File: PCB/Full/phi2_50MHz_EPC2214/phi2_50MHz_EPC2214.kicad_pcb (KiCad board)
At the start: 2 copper layers, 54 parts, among them J1 RF_IN, J2 RF_OUT, J5 Conn_01x01_Pin, J6 Conn_01x01_Pin, Q1 EPC2214, U1 TPS563203, U2 NC7WZ04, U3 NC7WZ04, U4 TLV3501, U5 NC7WZ04, U6 NC7WZ04, U7 NC7WZ04

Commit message: rough draft of phi 2 board
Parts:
- removed C16: C_Small, Capacitor_SMD:C_1206_3216Metric
- removed C30: C, Capacitor_SMD:C_0402_1005Metric
- removed U2: NC7WZ04, pcbparts:nc7wz04_sc-88_SOIC-6
- added D1: SMS3922, Diode_SMD:D_SOD-523, F.Cu at (134.7, 90.7)
- added D2: RB886GT2R, Diode_SMD:D_SOD-523, F.Cu at (134.7, 92.1)
- added D3: RB886GT2R, Diode_SMD:D_SOD-523, F.Cu at (134.7, 93.5)
- added D4: RB886GT2R, Diode_SMD:D_SOD-523, F.Cu at (134.7, 94.9)
- added D5: RB886GT2R, Diode_SMD:D_SOD-523, F.Cu at (137.3, 90.7)
- added D6: RB886GT2R, Diode_SMD:D_SOD-523, F.Cu at (137.3, 92.1)
- added D7: RB886GT2R, Diode_SMD:D_SOD-523, F.Cu at (137.3, 93.5)
- added D8: RB886GT2R, Diode_SMD:D_SOD-523, F.Cu at (137.3, 94.9)
- added REF**: MountingHole_4.3mm_M4_DIN965, MountingHole:MountingHole_4.3mm_M4_DIN965, F.Cu at (164.7, 61.8)
- added REF**: MountingHole_4.3mm_M4_DIN965, MountingHole:MountingHole_4.3mm_M4_DIN965, F.Cu at (106.7, 61.8)
- added REF**: MountingHole_4.3mm_M4_DIN965, MountingHole:MountingHole_4.3mm_M4_DIN965, F.Cu at (164.7, 119.8)
- added REF**: MountingHole_4.3mm_M4_DIN965, MountingHole:MountingHole_4.3mm_M4_DIN965, F.Cu at (106.7, 119.8)
- 12 V: renamed from J5
- C10: footprint Capacitor_SMD:C_0603_1608Metric -> Capacitor_SMD:C_0402_1005Metric
- moved RF_IN 86.4 mm to (136.3, 118.6), turned to 90 degrees
- moved GND 84.6 mm to (135.5, 74.3)
- moved C10 78.2 mm to (133.1, 111.8), turned to -90 degrees
- moved U4 75.3 mm to (135.3, 110.9), turned to 90 degrees
- moved R4 73.3 mm to (135.5, 113.7)
- moved C1 73.2 mm to (124.4, 70.9)
- moved R5 72.4 mm to (137.8, 110.9), turned to -90 degrees
- moved U3 70.1 mm to (135.9, 107.0), turned to 0 degrees
- moved R6 68.0 mm to (132.4, 113.7), turned to 180 degrees
- moved U5 63.5 mm to (133.6, 103.5), turned to 0 degrees
- moved U7 63.3 mm to (138.3, 103.5), turned to 0 degrees
- moved U6 63.2 mm to (135.9, 103.5), turned to 0 degrees
- moved C9 60.7 mm to (137.6, 107.5), turned to 90 degrees
- moved C4 60.7 mm to (124.5, 80.7), turned to 0 degrees
- moved C11 59.0 mm to (139.9, 104.1), turned to 90 degrees
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- renumbered J6 to GND, J1 to RF_IN, J2 to RF_OUT
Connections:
- C13 pad 1: Net-(C13-Pad1) -> /D
- C14 pad 1: Net-(C13-Pad1) -> /D
- C15 pad 1: Net-(C13-Pad2) -> /D
- C19 pad 1: Net-(C13-Pad2) -> /D
- C20 pad 1: Net-(C13-Pad2) -> /D
- L1 pad 2: Net-(C13-Pad1) -> /D
- L2 pad 1: Net-(C13-Pad1) -> /D
- Q1 pad 4: Net-(C13-Pad1) -> /D
- Q1 pad 5: Net-(C13-Pad1) -> /D
- Q1 pad 6: Net-(C13-Pad1) -> /D
- Q1 pad 7: Net-(C13-Pad1) -> /D
- U5 pad 4: /G -> /G1
- U5 pad 6: /G -> /G1
- U6 pad 4: /G -> /G1
- U6 pad 6: /G -> /G1
- U7 pad 4: /G -> /G1
- U7 pad 6: /G -> /G1
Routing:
- net +5V: track 0.00 -> 83.7 mm
- net /G1: track 0.00 -> 14.5 mm
- net Net-(U3-Y1): track 0.00 -> 13.0 mm
- net Net-(J2-In): track 0.00 -> 10.6 mm, vias 0 -> 7
- net Net-(U1-SW): track 0.00 -> 10.0 mm, vias 0 -> 2
- net Net-(U4--IN): track 0.00 -> 6.66 mm
- net /RF_IN: track 0.00 -> 6.63 mm
- net Net-(U1-EN): track 0.00 -> 5.70 mm
- net Net-(U1-FB): track 0.00 -> 4.31 mm
- net /D: track 0.00 -> 2.38 mm, vias 0 -> 12
- net GND: track 0.00 -> 1.68 mm, vias 0 -> 213
- net /G: track 0.00 -> 1.53 mm, vias 0 -> 9
- net Net-(U1-BST): track 0.00 -> 1.43 mm
- net Net-(C5-Pad1): vias 0 -> 3
- net Net-(C13-Pad2): vias 0 -> 6
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- added copper zone on F.Cu, net +12V
- added copper zone on F.Cu, net +5V
- added copper zone on B.Cu, net /D
- added copper zone on F.Cu, net /D
- added copper zone on B.Cu, net /G
- added copper zone on F.Cu, net /G
- added copper zone on F.Cu, net /G1
- added copper zone on B.Cu, net GND
- added copper zone on F.Cu, net GND
- added copper zone on B.Cu, net Net-(C12-Pad1)
- added copper zone on F.Cu, net Net-(C12-Pad1)
- added copper zone on B.Cu, net Net-(C13-Pad2)
- added copper zone on F.Cu, net Net-(C13-Pad2)
- added copper zone on B.Cu, net Net-(C5-Pad1)
- added copper zone on F.Cu, net Net-(C5-Pad1)
- added copper zone on B.Cu, net Net-(J2-In)
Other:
- board outline added: 70 x 70 mm
- board text added: "IMSSDC 6 50 MHz GaN PA CALVIN H LIN, ZHECHI YE"

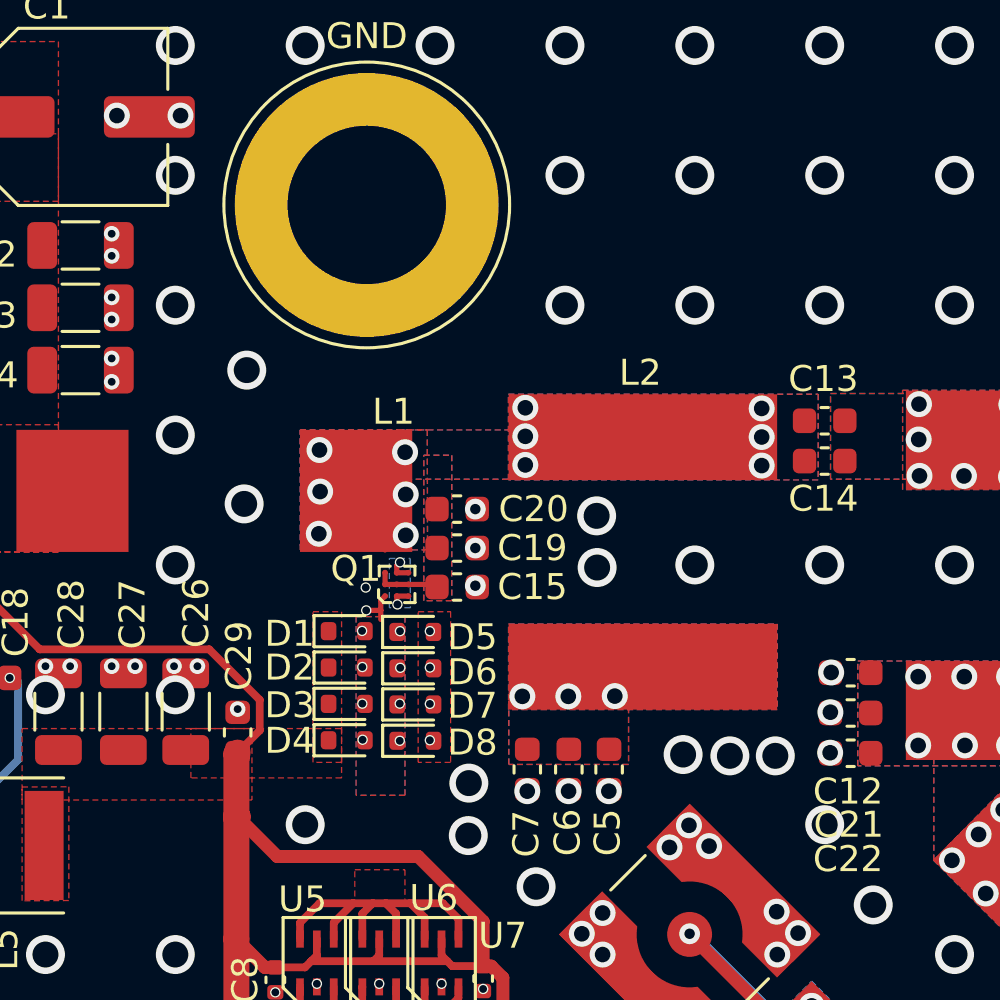
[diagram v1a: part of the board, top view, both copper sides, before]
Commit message: deleted some vias
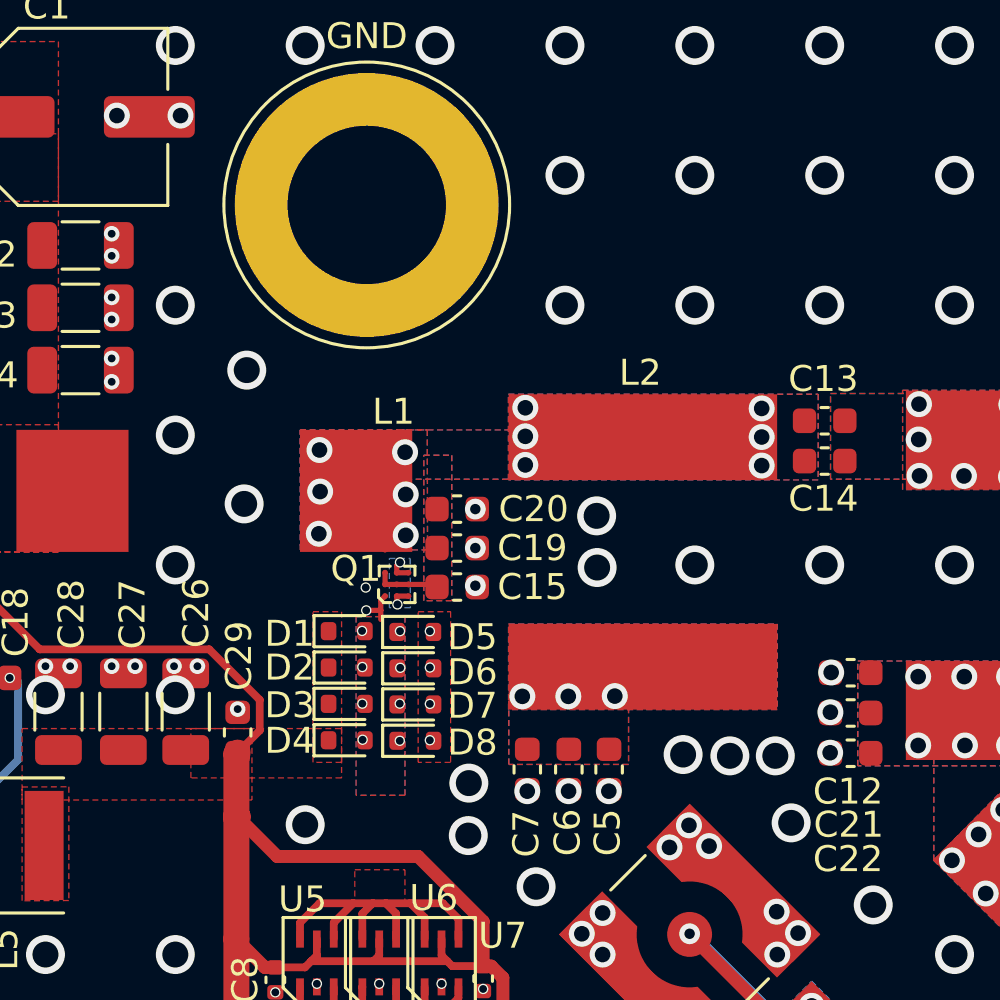
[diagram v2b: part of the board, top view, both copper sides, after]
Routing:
- net GND: vias 213 -> 212
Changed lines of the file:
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@@
 	)
 	(via
-		(at 153.1 98.15)
+		(at 151.81 98.08)
 		(size 1.5)
 		(drill 1)
@@
 		(size 1.5)
 		(drill 1)
-		(layers "F.Cu" "B.Cu")
-		(free yes)
-		(net 1)
-	)
-	(via
-		(at 128.1 73.15)
-		(size 1.5)
-		(drill 1)

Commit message: gerbers and rev1 board sent out
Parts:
- removed the REF** at (164.7, 61.8)
- removed the REF** at (106.7, 61.8)
- removed the REF** at (164.7, 119.8)
- removed the REF** at (106.7, 119.8)
- added G***: LOGO, Logo:superlab_logo, F.Cu at (74.3, 81.8)
- added REF**: MountingHole_3.2mm_M3_DIN965, MountingHole:MountingHole_3.2mm_M3_DIN965, F.Cu at (4.67, 84.8)
- added REF**: MountingHole_3.2mm_M3_DIN965, MountingHole:MountingHole_3.2mm_M3_DIN965, F.Cu at (84.7, 41.7)
- added REF**: MountingHole_3.2mm_M3_DIN965, MountingHole:MountingHole_3.2mm_M3_DIN965, F.Cu at (84.7, 3.80)
- added REF**: MountingHole_3.2mm_M3_DIN965, MountingHole:MountingHole_3.2mm_M3_DIN965, F.Cu at (4.67, 3.80)
- added REF**: MountingHole_3.2mm_M3_DIN965, MountingHole:MountingHole_3.2mm_M3_DIN965, F.Cu at (84.7, 84.8)
- added REF**: MountingHole_3.2mm_M3_DIN965, MountingHole:MountingHole_3.2mm_M3_DIN965, F.Cu at (4.67, 41.7)
- moved C15 108.3 mm to (45.6, 34.0), turned to -90 degrees
- moved C1 107.4 mm to (31.8, 16.6)
- moved C10 107.4 mm to (40.4, 57.5)
- moved C25 107.4 mm to (24.8, 42.5)
- moved C5 107.4 mm to (52.2, 41.7)
- moved R5 107.4 mm to (45.2, 56.6)
- moved RF_IN 107.4 mm to (43.7, 64.3)
- moved U4 107.4 mm to (42.7, 56.6)
- moved U5 107.4 mm to (40.9, 49.2)
- moved 12 V 107.4 mm to (21.2, 15.7)
- moved C11 107.4 mm to (47.3, 49.8)
- moved C12 107.4 mm to (61.5, 38.0)
- moved C13 107.4 mm to (60.5, 28.3)
- moved C14 107.4 mm to (60.5, 29.9)
- moved C17 107.4 mm to (41.5, 53.3)
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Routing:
- net +12V: track 0.19 -> 6.13 mm, vias 0 -> 2
- net Net-(J2-In): track 10.6 -> 5.35 mm, vias 7 -> 0
- net +5V: track 83.7 -> 85.7 mm
- net Net-(U3-A1): track 0.00 -> 1.98 mm
- net GND: track 1.68 -> 1.91 mm, vias 212 -> 210
- net /D: track 2.38 -> 2.61 mm, vias 12 -> 0
- net Net-(C5-Pad1): vias 3 -> 0
- net Net-(C13-Pad2): vias 6 -> 0
- net Net-(C12-Pad1): vias 12 -> 0
- added copper zone on F.Cu, net Net-(J2-In)
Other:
- board size 70 x 70 mm -> 89 x 89 mm
- board text added: "IMSSDC 6 2024 50 MHz GaN PA CALVIN H LIN, ZHECHI YE STANFORD POWER ELECTRONICS"
- board text removed: "IMSSDC 6 50 MHz GaN PA CALVIN H LIN, ZHECHI YE"

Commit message: added width to drain trace, now sent out board
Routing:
- net /D: track 2.61 -> 4.05 mm
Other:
- board text added: "IMS SDC6 2024 50 MHz GaN PA CALVIN H LIN, ZHECHI YE STANFORD POWER ELECTRONICS"
- board text removed: "IMSSDC 6 2024 50 MHz GaN PA CALVIN H LIN, ZHECHI YE STANFORD POWER ELECTRONICS"
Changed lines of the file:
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@@
 			(fill solid)
 			(layer "F.SilkS")
-			(net 45360009)
 		)
 		(fp_poly
@@
 		(layer "Edge.Cuts")
 	)
-	(gr_text "IMSSDC 6 2024\n50 MHz GaN PA\nCALVIN H LIN, ZHECHI YE\nSTANFORD POWER ELECTRONICS"
+	(gr_text "IMS SDC6 2024\n50 MHz GaN PA\nCALVIN H LIN, ZHECHI YE\nSTANFORD POWER ELECTRONICS"
 		(at 45.855 85.35 0)
 		(layer "F.SilkS")
@@
 	)
 	(via
-		(at 42.78 34.23)
+		(at 42.48 34.36)
 		(size 0.4)
 		(drill 0.3)
@@
 	)
 	(segment
+		(start 42.41 31.11)
+		(end 43.43 32.13)
+		(width 0.5)
+		(layer "F.Cu")
+		(net 6)
+	)
+	(segment
 		(start 45.74 33.17)
 		(end 45.71 33.2)
@@
 	)
 	(zone
+		(net 9)
+		(net_name "Net-(U1-SW)")
+		(layer "F.Cu")
+		(name "$teardrop_padvia$")
+		(hatch full 0.1)
+		(priority 30000)
+		(attr
+			(teardrop
+				(type padvia)
+			)
+		)
+		(connect_pads yes
+			(clearance 0)
+		)
+		(min_thickness 0.0254)
+		(filled_areas_thickness no)
+		(fill yes
+			(thermal_gap 0.5)
+			(thermal_bridge_width 0.5)
+			(island_removal_mode 1)
+			(island_area_min 10)
+		)
+		(polygon
+			(pts
+				(xy 26.57 41.69) (xy 26.87 41.69) (xy 26.89 41.435) (xy 26.72 41.169) (xy 26.55 41.435)
+			)
+		)
+	)
+	(zone
 		(net 1)
 		(net_name "GND")
@@
 	)
 	(zone
-		(net 9)
-		(net_name "Net-(U1-SW)")
+		(net 2)
+		(net_name "+12V")
 		(layer "F.Cu")
-		(name "$teardrop_padvia$")
-		(hatch full 0.1)
-		(priority 30000)
-		(attr
-			(teardrop
-				(type padvia)
-			)
-		)
+		(hatch edge 0.5)
+		(priority 1)
 		(connect_pads yes
-			(clearance 0)
+			(clearance 0.1)
 		)
-		(min_thickness 0.0254)
+		(min_thickness 0.25)
 		(filled_areas_thickness no)
 		(fill yes
 			(thermal_gap 0.5)
 			(thermal_bridge_width 0.5)
-			(island_removal_mode 1)
-			(island_area_min 10)
 		)
 		(polygon
 			(pts
-				(xy 26.57 41.69) (xy 26.87 41.69) (xy 26.89 41.435) (xy 26.72 41.169) (xy 26.55 41.435)
+				(xy 30.97 33.37) (xy 18.97 33.37) (xy 18.97 28.47) (xy 30.97 28.47)
 			)
 		)
 	)
 	(zone
-		(net 2)
-		(net_name "+12V")
+		(net 4)
+		(net_name "+5V")
 		(layer "F.Cu")
 		(hatch edge 0.5)
-		(priority 1)
 		(connect_pads yes
 			(clearance 0.1)
@@
 		(polygon
 			(pts
-				(xy 30.97 33.37) (xy 18.97 33.37) (xy 18.97 28.47) (xy 30.97 28.47)
+				(xy 41.87 42.07) (xy 36.07 42.07) (xy 36.07 40.17) (xy 41.87 40.17)
 			)
 		)
 	)
 	(zone
-		(net 4)
-		(net_name "+5V")
+		(net 6)
+		(net_name "/D")
 		(layer "F.Cu")
 		(hatch edge 0.5)
+		(priority 7)
 		(connect_pads yes
-			(clearance 0.1)
+			(clearance 0)
 		)
 		(min_thickness 0.25)
@@
 		(polygon
 			(pts
-				(xy 41.87 42.07) (xy 36.07 42.07) (xy 36.07 40.17) (xy 41.87 40.17)
+				(xy 43.09 33.39) (xy 43.65 33.39) (xy 43.65 34.71) (xy 43.09 34.71)
 			)
 		)
@@
 		(polygon
 			(pts
-				(xy 43.42 33.76) (xy 43.66 33.76) (xy 43.66 34.73) (xy 43.42 34.73)
+				(xy 43.09 33.42) (xy 43.68 33.42) (xy 43.68 34.73) (xy 43.09 34.73)
 			)
 		)

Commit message: kicad changes if i ever make a new board
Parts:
- moved R3 0.27 mm to (24.3, 35.1)
- moved R7 0.27 mm to (24.3, 38.2)
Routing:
- net (no net): track 0.00 -> 1.34 mm
- net GND: track 1.91 -> 2.83 mm
- net +12V: track 6.13 -> 5.31 mm, vias 2 -> 1
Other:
- board text added: "Check ground pin of IC does ground need to be connected underneath package? should we use a different 0.1 uF capacitor with higher voltage rating? 4.7 uH"
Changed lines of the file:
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@@
 	(footprint "Resistor_SMD:R_0603_1608Metric"
 		(layer "F.Cu")
-		(at 24.57 38.32 -90)
+		(at 24.32 38.22 -90)
 		(descr "Resistor SMD 0603 (1608 Metric), square (rectangular) end terminal, IPC_7351 nominal, (Body size source: IPC-SM-782 page 72, https://www.pcb-3d.com/wordpress/wp-content/uploads/ipc-sm-782a_amendment_1_and_2.pdf), generated with kicad-footprint-generator")
 		(tags "resistor")
@@
 	(footprint "Resistor_SMD:R_0603_1608Metric"
 		(layer "F.Cu")
-		(at 24.57 35.22 -90)
+		(at 24.32 35.12 -90)
 		(descr "Resistor SMD 0603 (1608 Metric), square (rectangular) end terminal, IPC_7351 nominal, (Body size source: IPC-SM-782 page 72, https://www.pcb-3d.com/wordpress/wp-content/uploads/ipc-sm-782a_amendment_1_and_2.pdf), generated with kicad-footprint-generator")
 		(tags "resistor")
@@
 		)
 	)
+	(gr_text "Check ground pin of IC\ndoes ground need to be connected underneath package?\nshould we use a different 0.1 uF capacitor with higher voltage rating?\n4.7 uH"
+		(at 10.94 101.94 0)
+		(layer "Cmts.User")
+		(effects
+			(font
+				(size 1.5 1.5)
+				(thickness 0.3)
+				(bold yes)
+			)
+			(justify left bottom)
+		)
+	)
+	(segment
+		(start 26.95 40.34)
+		(end 27.08 40.47)
+		(width 0.25)
+		(layer "F.Cu")
+		(net 0)
+	)
+	(segment
+		(start 25.79 40.34)
+		(end 26.95 40.34)
+		(width 0.25)
+		(layer "F.Cu")
+		(net 0)
+	)
 	(segment
 		(start 43.995 35.07)
@@
 	)
 	(segment
+		(start 27.92 41.17)
+		(end 28.07 41.32)
+		(width 0.25)
+		(layer "F.Cu")
+		(net 1)
+	)
+	(segment
 		(start 43.976666 35.346266)
 		(end 43.995 35.327932)
@@
 	)
 	(segment
+		(start 27.22 41.17)
+		(end 27.92 41.17)
+		(width 0.25)
+		(layer "F.Cu")
+		(net 1)
+	)
+	(segment
 		(start 43.995 34.17)
 		(end 44.44 34.17)
@@
 	(segment
 		(start 25.97 36.88)
-		(end 25.97 37.89)
-		(width 0.3)
+		(end 25.145 36.055)
+		(width 0.25)
 		(layer "F.Cu")
 		(net 2)
 	)
 	(segment
-		(start 25.97 37.89)
-		(end 26.01 37.93)
-		(width 0.3)
+		(start 31.645 30.885)
+		(end 31.51 31.02)
+		(width 1.5)
 		(layer "F.Cu")
 		(net 2)
 	)
 	(segment
-		(start 31.645 30.885)
-		(end 31.51 31.02)
-		(width 1.5)
+		(start 24.78 35.15)
+		(end 23.45 35.15)
+		(width 0.25)
+		(layer "F.Cu")
+		(net 2)
+	)
+	(segment
+		(start 25.145 36.055)
+		(end 25.145 35.515)
+		(width 0.25)
 		(layer "F.Cu")
 		(net 2)
@@
 		(net 2)
 	)
-	(via
-		(at 26.15 41.18)
-		(size 0.4)
-		(drill 0.3)
-		(layers "F.Cu" "B.Cu")
+	(segment
+		(start 25.145 35.515)
+		(end 24.78 35.15)
+		(width 0.25)
+		(layer "F.Cu")
 		(net 2)
 	)
 	(via
-		(at 26.01 37.93)
-		(size 0.6)
+		(at 26.15 41.18)
+		(size 0.4)
 		(drill 0.3)
 		(layers "F.Cu" "B.Cu")
-		(free yes)
-		(net 2)
-	)
-	(segment
-		(start 26.01 41.04)
-		(end 26.01 37.93)
-		(width 0.3)
-		(layer "B.Cu")
-		(net 2)
-	)
-	(segment
-		(start 26.15 41.18)
-		(end 26.01 41.04)
-		(width 0.3)
-		(layer "B.Cu")
 		(net 2)
 	)
@@
 	)
 	(zone
-		(net 9)
-		(net_name "Net-(U1-SW)")
-		(layer "F.Cu")
-		(name "$teardrop_padvia$")
-		(hatch full 0.1)
-		(priority 30000)
-		(attr
-			(teardrop
-				(type padvia)
-			)
-		)
-		(connect_pads yes
-			(clearance 0)
-		)
-		(min_thickness 0.0254)
-		(filled_areas_thickness no)
-		(fill yes
-			(thermal_gap 0.5)
-			(thermal_bridge_width 0.5)
-			(island_removal_mode 1)
-			(island_area_min 10)
-		)
-		(polygon
-			(pts
-				(xy 26.57 41.69) (xy 26.87 41.69) (xy 26.89 41.435) (xy 26.72 41.169) (xy 26.55 41.435)
-			)
-		)
-	)
-	(zone
 		(net 1)
 		(net_name "GND")
@@
 			)
 		)
+	)
+	(zone
+		(net 9)
+		(net_name "Net-(U1-SW)")
+		(layer "F.Cu")
+		(name "$teardrop_padvia$")
+		(hatch full 0.1)
+		(priority 30000)
+		(attr
+			(teardrop
+				(type padvia)
+			)
+		)
+		(connect_pads yes
+			(clearance 0)
+		)
+		(min_thickness 0.0254)
+		(filled_areas_thickness no)
+		(fill yes
+			(thermal_gap 0.5)
+			(thermal_bridge_width 0.5)
+			(island_removal_mode 1)
+			(island_area_min 10)
+		)
+		(polygon
+			(pts
+				(xy 26.57 41.69) (xy 26.87 41.69) (xy 26.89 41.435) (xy 26.72 41.169) (xy 26.55 41.435)
+			)
+		)

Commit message: ims changes
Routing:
- net (no net): track 1.34 -> 0.00 mm
- net GND: track 2.83 -> 4.17 mm
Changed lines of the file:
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@@
+	)
+	(segment
+		(start 43.995 35.07)
+		(end 44.43 35.07)
+		(width 0.2)
+		(layer "F.Cu")
+		(net 1)
 	)
 	(segment
@@
 		(end 27.08 40.47)
 		(width 0.25)
-		(layer "F.Cu")
-		(net 0)
-	)
-	(segment
-		(start 25.79 40.34)
-		(end 26.95 40.34)
-		(width 0.25)
-		(layer "F.Cu")
-		(net 0)
-	)
-	(segment
-		(start 43.995 35.07)
-		(end 44.43 35.07)
-		(width 0.2)
 		(layer "F.Cu")
 		(net 1)
@@
 		(width 0.25)
 		(layer "F.Cu")
+		(net 1)
+	)
+	(segment
+		(start 25.79 40.34)
+		(end 26.95 40.34)
+		(width 0.25)
+		(layer "F.Cu")
